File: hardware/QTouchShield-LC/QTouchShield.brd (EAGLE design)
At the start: 101.6 x 81.3 mm, 59 parts, among them IC1 AT32UC3C0512CJEDEC-MS-026, J1 SENSOR 00...07, J10 CAP 08...15, J11 CAP 16...23, J12 CAP 24...31, J13 SPI-MEGA, J14 SPI-UNO, J15 COMMS Select, J16 DETECT00...15, J17 DETECT16...31, J18 JTAG, J19 TOUCH DATA, J2 SENSOR 08...15, J3 SENSOR 16...23, J4 SENSOR 24...31, J5 RES 00...07, J6 RES 08...15, J7 RES 16...23, J8 RES 24...31, J9 CAP 00...07, Q1 BSS138, Q2 BSS138, Q3 BSS138, Q4 BSS138, Q5 BSS138, Q6 BSS138, U1 ARDUINO-2560-MEGA-R3-SMD, X1 Firmware Upgrade Port

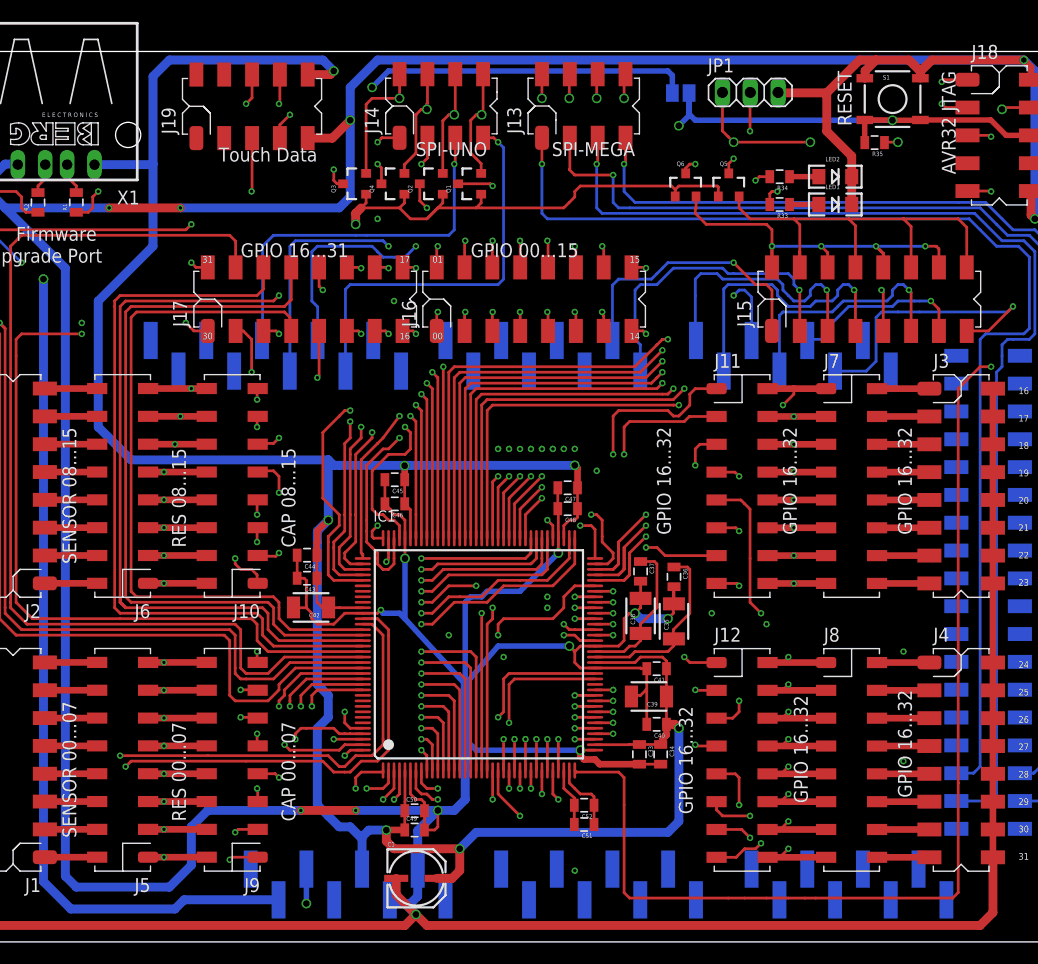
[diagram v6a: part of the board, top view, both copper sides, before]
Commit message: Updated schematic and board, especially silk screen
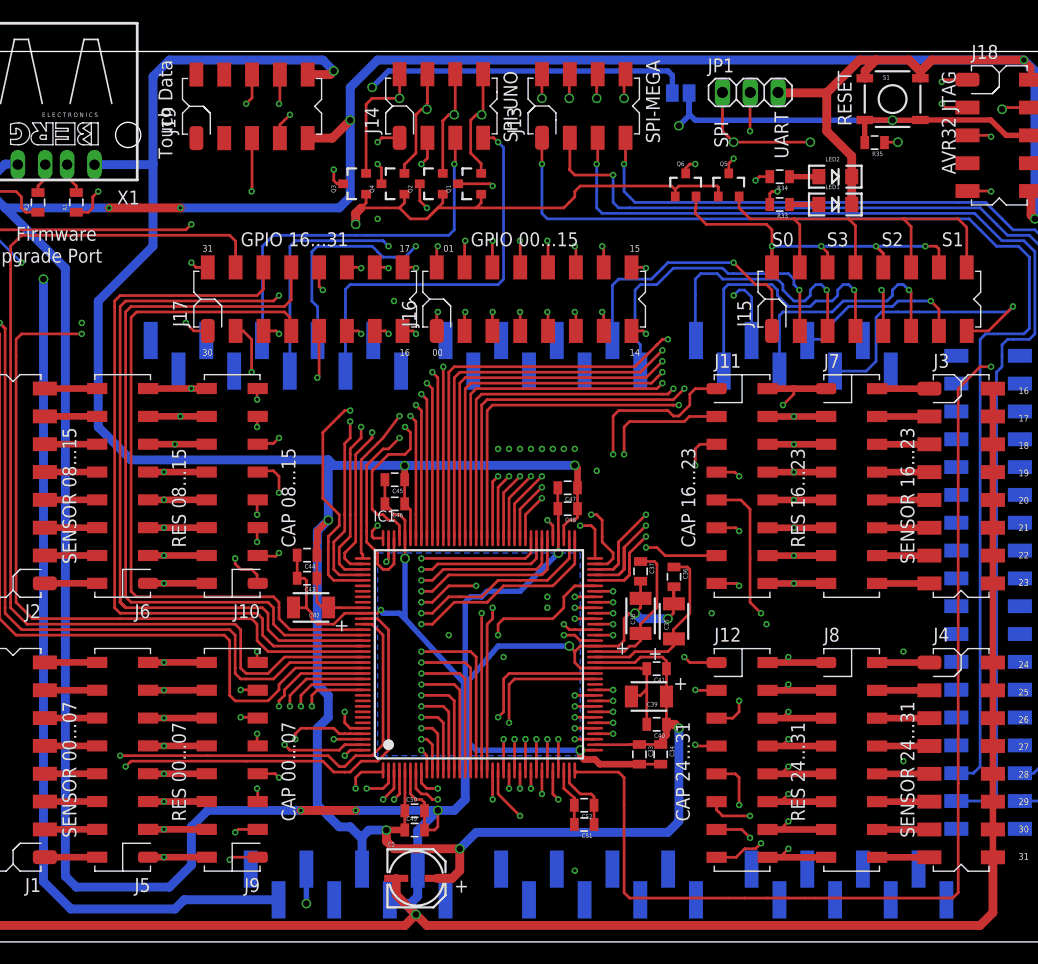
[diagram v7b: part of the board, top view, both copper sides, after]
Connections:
- net SPI-MISO-ALT renamed MISO-UNO
- net SPI-MOSI-ALT renamed MOSI-UNO
- net SPI-SCK-ALT renamed SCK-UNO
- net SPI-SS-ALT renamed SS-UNO
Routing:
- net N$34: track 2.90 -> 4.01 mm
- added copper zone on layer 16, net GND
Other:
- board text added: "+"
- board text added: "CAP 16...23"
- board text added: "CAP 24...31"
- board text added: "RES 16...23"
- board text added: "RES 24...31"
- board text added: "S0"
- board text added: "S1"
- board text added: "S2"
- board text added: "S3"
- board text added: "SENSOR 16...23"
- board text added: "SENSOR 24...31"
- board text added: "SPI"
- board text added: "UART"
- board text removed: "GPIO 16...32"
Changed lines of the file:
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@@
 <layer number="23" name="tOrigins" color="15" fill="1" visible="no" active="yes"/>
 <layer number="24" name="bOrigins" color="15" fill="1" visible="yes" active="yes"/>
-<layer number="25" name="tNames" color="7" fill="1" visible="no" active="yes"/>
+<layer number="25" name="tNames" color="7" fill="1" visible="yes" active="yes"/>
 <layer number="26" name="bNames" color="7" fill="1" visible="yes" active="yes"/>
-<layer number="27" name="tValues" color="7" fill="1" visible="yes" active="yes"/>
+<layer number="27" name="tValues" color="7" fill="1" visible="no" active="yes"/>
 <layer number="28" name="bValues" color="7" fill="1" visible="yes" active="yes"/>
 <layer number="29" name="tStop" color="7" fill="3" visible="no" active="yes"/>
@@
 <wire x1="101.6" y1="81.28" x2="0" y2="81.28" width="0" layer="20"/>
 <wire x1="0" y1="81.28" x2="0" y2="0" width="0" layer="20"/>
-<text x="34" y="72.5" size="1.27" layer="21" font="vector" rot="R180">Touch Data</text>
-<text x="49.5" y="73" size="1.27" layer="21" font="vector" rot="R180">SPI-UNO</text>
-<text x="63" y="73" size="1.27" layer="21" font="vector" rot="R180">SPI-MEGA</text>
+<text x="19.5" y="80.5" size="1.27" layer="21" font="vector" rot="R270">Touch Data</text>
+<text x="51" y="79.5" size="1.27" layer="21" font="vector" rot="R270">SPI-UNO</text>
+<text x="64" y="80.5" size="1.27" layer="21" font="vector" rot="R270">SPI-MEGA</text>
 <text x="81.5" y="79.5" size="1.27" layer="21" font="vector" rot="R270">RESET</text>
 <text x="91" y="79.5" size="1.27" layer="21" font="vector" rot="R270">AVR32 JTAG</text>
 <text x="6.5" y="64" size="1.27" layer="21" font="vector">Firmware</text>
 <text x="4" y="62" size="1.27" layer="21" font="vector">Upgrade Port</text>
-<text x="27" y="62.5" size="1.27" layer="21" font="vector">GPIO 16...31</text>
-<text x="48" y="62.5" size="1.27" layer="21" font="vector">GPIO 00...15</text>
-<text x="65" y="47" size="1.27" layer="21" font="vector" rot="R270">GPIO 16...32</text>
-<text x="76.5" y="47" size="1.27" layer="21" font="vector" rot="R270">GPIO 16...32</text>
-<text x="87" y="47" size="1.27" layer="21" font="vector" rot="R270">GPIO 16...32</text>
-<text x="67" y="21.5" size="1.27" layer="21" font="vector" rot="R270">GPIO 16...32</text>
-<text x="77.5" y="22.5" size="1.27" layer="21" font="vector" rot="R270">GPIO 16...32</text>
-<text x="87" y="23" size="1.27" layer="21" font="vector" rot="R270">GPIO 16...32</text>
+<text x="27" y="63.5" size="1.27" layer="21" font="vector">GPIO 16...31</text>
+<text x="48" y="63.5" size="1.27" layer="21" font="vector">GPIO 00...15</text>
+<text x="68.5" y="36" size="1.27" layer="21" font="vector" rot="R90">CAP 16...23</text>
+<text x="78.5" y="36" size="1.27" layer="21" font="vector" rot="R90">RES 16...23</text>
+<text x="88.5" y="34.5" size="1.27" layer="21" font="vector" rot="R90">SENSOR 16...23</text>
+<text x="68" y="11" size="1.27" layer="21" font="vector" rot="R90">CAP 24...31</text>
+<text x="78.5" y="11" size="1.27" layer="21" font="vector" rot="R90">RES 24...31</text>
+<text x="88.5" y="9.5" size="1.27" layer="21" font="vector" rot="R90">SENSOR 24...31</text>
 <text x="12" y="9.5" size="1.27" layer="21" font="vector" rot="R90">SENSOR 00...07</text>
 <text x="22" y="11" size="1.27" layer="21" font="vector" rot="R90">RES 00...07</text>
 <text x="32" y="11" size="1.27" layer="21" font="vector" rot="R90">CAP 00...07</text>
-<text x="23.5" y="55" size="0.6096" layer="21" font="vector">30</text>
-<text x="23.5" y="62" size="0.6096" layer="21" font="vector">31</text>
-<text x="41.5" y="55" size="0.6096" layer="21" font="vector">16</text>
-<text x="41.5" y="62" size="0.6096" layer="21" font="vector">17</text>
-<text x="44.5" y="62" size="0.6096" layer="21" font="vector">01</text>
-<text x="44.5" y="55" size="0.6096" layer="21" font="vector">00</text>
-<text x="62.5" y="62" size="0.6096" layer="21" font="vector">15</text>
-<text x="62.5" y="55" size="0.6096" layer="21" font="vector">14</text>
+<text x="23.5" y="53.5" size="0.6096" layer="21" font="vector">30</text>
+<text x="23.5" y="63" size="0.6096" layer="21" font="vector">31</text>
+<text x="41.5" y="53.5" size="0.6096" layer="21" font="vector">16</text>
+<text x="41.5" y="63" size="0.6096" layer="21" font="vector">17</text>
+<text x="45.5" y="63" size="0.6096" layer="21" font="vector">01</text>
+<text x="44.5" y="53.5" size="0.6096" layer="21" font="vector">00</text>
+<text x="62.5" y="63" size="0.6096" layer="21" font="vector">15</text>
+<text x="62.5" y="53.5" size="0.6096" layer="21" font="vector">14</text>
 <text x="1" y="7.5" size="0.6096" layer="21" font="vector">00</text>
 <text x="1" y="10" size="0.6096" layer="21" font="vector">01</text>
@@
 <text x="98" y="47.5" size="0.6096" layer="21" font="vector">17</text>
 <text x="98" y="50" size="0.6096" layer="21" font="vector">16</text>
+<text x="71.5" y="72.5" size="1.27" layer="21" font="vector" rot="R90">SPI</text>
+<text x="77" y="71.5" size="1.27" layer="21" font="vector" rot="R90">UART</text>
+<text x="75.5" y="63.5" size="1.27" layer="21" font="vector">S0</text>
+<text x="80.5" y="63.5" size="1.27" layer="21" font="vector">S3</text>
+<text x="85.5" y="63.5" size="1.27" layer="21" font="vector">S2</text>
+<text x="91" y="63.5" size="1.27" layer="21" font="vector">S1</text>
+<text x="46.5" y="4.5" size="1.27" layer="21">+</text>
+<text x="66.5" y="23" size="1.27" layer="21">+</text>
+<text x="65.5" y="27" size="1.27" layer="21" rot="R180">+</text>
+<text x="62.5" y="27.5" size="1.27" layer="21" rot="R180">+</text>
+<text x="35.5" y="29.5" size="1.27" layer="21" rot="R270">+</text>
 </plain>
 <attributes>
@@
 <wire x1="58" y1="17" x2="58" y2="17.5" width="0.6096" layer="1"/>
 <wire x1="59.35" y1="17.5" x2="58" y2="17.5" width="0.254" layer="1"/>
+<polygon width="0.254" layer="16">
+<vertex x="39.5" y="35.5"/>
+<vertex x="58" y="35.5"/>
+<vertex x="58" y="17"/>
+<vertex x="39.5" y="17"/>
+</polygon>
 <wire x1="31.853" y1="30.5" x2="31.825" y2="30.528" width="0" layer="19" extent="1-1"/>
 </signal>
@@
 <wire x1="36" y1="49" x2="36" y2="47.5" width="0.254" layer="15"/>
 </signal>
-<signal name="SPI-SCK-ALT">
+<signal name="SCK-UNO">
 <contactref element="U1" pad="PWM13"/>
 <contactref element="J14" pad="5"/>
@@
 <wire x1="46.59" y1="71.09" x2="46.59" y2="73.4" width="0.254" layer="1"/>
 </signal>
-<signal name="SPI-MISO-ALT">
+<signal name="MISO-UNO">
 <contactref element="U1" pad="PWM12"/>
 <contactref element="J14" pad="1"/>
@@
 <wire x1="39.9" y1="73.4" x2="41.51" y2="73.4" width="0.254" layer="1"/>
 </signal>
-<signal name="SPI-MOSI-ALT">
+<signal name="MOSI-UNO">
 <contactref element="U1" pad="PWM11"/>
 <contactref element="J14" pad="3"/>
@@
 <wire x1="44.05" y1="71.55" x2="44.05" y2="73.4" width="0.254" layer="1"/>
 </signal>
-<signal name="SPI-SS-ALT">
+<signal name="SS-UNO">
 <contactref element="U1" pad="PWM10"/>
 <contactref element="J14" pad="7"/>
@@
 <wire x1="12" y1="69" x2="11.16" y2="69.84" width="0.254" layer="1"/>
 <wire x1="11.16" y1="69.84" x2="11.16" y2="70.95" width="0.254" layer="1"/>
+<wire x1="11.16" y1="69.84" x2="11.16" y2="70.95" width="0.254" layer="1"/>
 </signal>
